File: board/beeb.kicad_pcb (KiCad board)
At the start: 2 copper layers, 59.7 x 53.3 mm, 24 parts, among them J2 AVR-JTAG-10, SW1 SW_DIP_x08, U2 ps2, U3 XC95144XL-TQ100, U4 beebKB, U5 OKI-78SR-3.3_1.5-W36-C

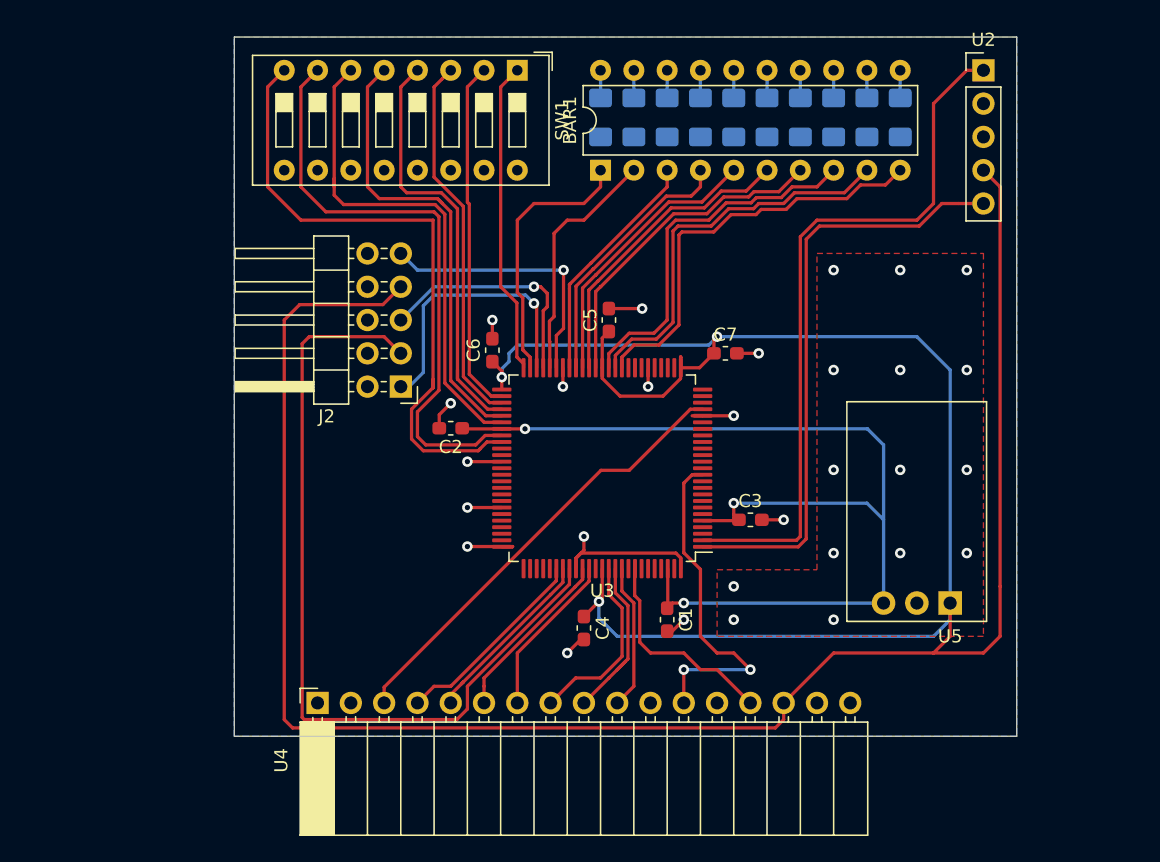
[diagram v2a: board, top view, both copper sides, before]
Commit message: Add ps/2 socket footprint from github. Add USB socket via WIT122 IC.
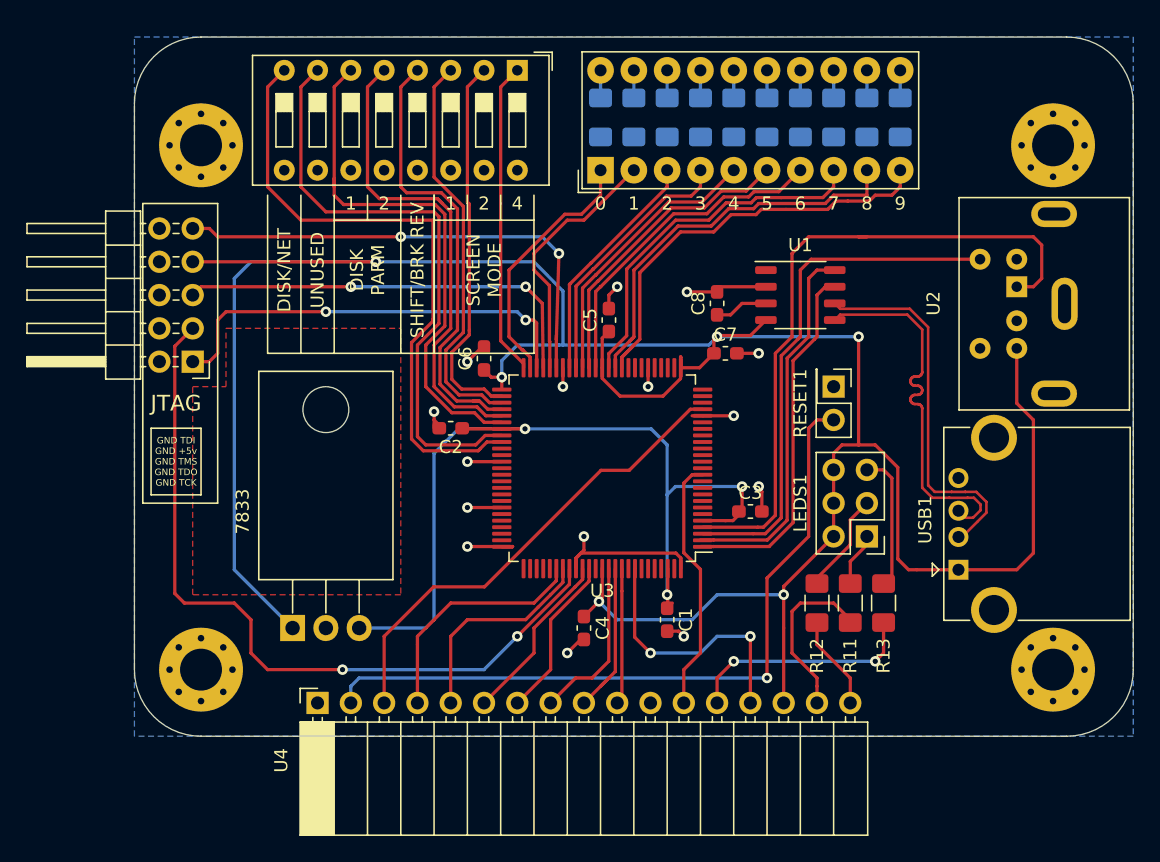
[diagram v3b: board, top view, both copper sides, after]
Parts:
- added C8: 0.1uF, Capacitor_SMD:C_0603_1608Metric_Pad1.05x0.95mm_HandSolder, F.Cu at (91.4, 99.1)
- added H1: MountingHole_Pad, MountingHole:MountingHole_3.2mm_M3_Pad_Via, F.Cu at (117.1, 127.0)
- added H2: MountingHole_Pad, MountingHole:MountingHole_3.2mm_M3_Pad_Via, F.Cu at (117.1, 87.0)
- added H3: MountingHole_Pad, MountingHole:MountingHole_3.2mm_M3_Pad_Via, F.Cu at (52.1, 127.0)
- added H4: MountingHole_Pad, MountingHole:MountingHole_3.2mm_M3_Pad_Via, F.Cu at (52.1, 87.0)
- added LEDS1: J1, Connector_PinHeader_2.54mm:PinHeader_2x03_P2.54mm_Vertical, F.Cu at (102.9, 116.8)
- added R11: 470, Resistor_SMD:R_1206_3216Metric_Pad1.42x1.75mm_HandSolder, F.Cu at (101.6, 121.9)
- added R12: 470, Resistor_SMD:R_1206_3216Metric_Pad1.42x1.75mm_HandSolder, F.Cu at (99.1, 121.9)
- added R13: 470, Resistor_SMD:R_1206_3216Metric_Pad1.42x1.75mm_HandSolder, F.Cu at (104.1, 121.9)
- added RESET1: J3, Connector_PinHeader_2.54mm:PinHeader_2x01_P2.54mm_Vertical, F.Cu at (100.3, 105.4)
- added U1: WIT122UH, Package_SO:SOP-8_3.9x4.9mm_P1.27mm, F.Cu at (97.8, 98.4)
- added USB1: USB, Connector_USB:USB_A_CONNFLY_DS1095-WNR0, F.Cu at (109.9, 119.4)
- BAR1: footprint Package_DIP:DIP-20_W7.62mm -> Display:HDSP-4830
- U2: footprint Connector_PinHeader_2.54mm:PinHeader_1x05_P2.54mm_Vertical -> thirdparty:Connector_Mini-DIN_Female_6Pin_2rows
- U5: value OKI-78SR-3.3_1.5-W36-C -> 7833; footprint Converter_DCDC:Converter_DCDC_muRata_OKI-78SR_Horizontal -> Package_TO_SOT_THT:TO-220-3_Horizontal_TabDown
- moved U5 50.2 mm to (59.1, 123.8), turned to 0 degrees
- moved U2 16.7 mm to (114.3, 97.8), turned to 90 degrees
- moved J2 16.0 mm to (51.4, 103.5)
- moved C6 0.90 mm to (73.7, 103.3)
- moved C3 0.63 mm to (94.0, 114.9)
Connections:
- J2 pad 4: Net-(J2-Pad4) -> (no net)
- J2 pad 6: Net-(J2-Pad6) -> (no net)
- J2 pad 8: Net-(J2-Pad8) -> (no net)
- U2 pad 1: Net-(U2-Pad1) -> /PS2DATA_A
- U2 pad 5: Net-(U2-Pad5) -> /PS2CLK_A
- U3 pad 1: Net-(U2-Pad5) -> /PS2DATA_B
- U3 pad 10: Net-(U3-Pad10) -> (no net)
- U3 pad 11: Net-(U3-Pad11) -> (no net)
- U3 pad 13: Net-(U3-Pad13) -> (no net)
- U3 pad 14: Net-(U3-Pad14) -> (no net)
- U3 pad 15: Net-(U3-Pad15) -> (no net)
- U3 pad 16: Net-(U3-Pad16) -> (no net)
- U3 pad 17: Net-(U3-Pad17) -> (no net)
- U3 pad 18: Net-(U3-Pad18) -> (no net)
- U3 pad 19: Net-(U3-Pad19) -> (no net)
- U3 pad 2: Net-(U2-Pad1) -> /PS2CLK_B
- U3 pad 20: Net-(U3-Pad20) -> (no net)
- U3 pad 23: Net-(U3-Pad23) -> (no net)
- U3 pad 24: Net-(U3-Pad24) -> (no net)
- U3 pad 25: Net-(U3-Pad25) -> (no net)
- U3 pad 27: Net-(U3-Pad27) -> (no net)
- U3 pad 28: Net-(U3-Pad28) -> (no net)
- U3 pad 29: Net-(U3-Pad29) -> (no net)
- U3 pad 3: Net-(U3-Pad3) -> /PS2CLK_A
- U3 pad 30: Net-(U3-Pad30) -> (no net)
- U3 pad 32: Net-(U3-Pad32) -> (no net)
- U3 pad 33: Net-(U3-Pad33) -> (no net)
- U3 pad 34: Net-(U3-Pad34) -> (no net)
- U3 pad 4: Net-(U3-Pad4) -> /PS2DATA_A
- U3 pad 6: Net-(U3-Pad6) -> (no net)
- U3 pad 60: Net-(U3-Pad60) -> (no net)
- U3 pad 61: Net-(U3-Pad61) -> (no net)
- U3 pad 63: Net-(U3-Pad63) -> (no net)
- U3 pad 64: Net-(U3-Pad64) -> (no net)
- U3 pad 65: Net-(U3-Pad65) -> (no net)
- U3 pad 66: Net-(U3-Pad66) -> (no net)
- U3 pad 67: Net-(U3-Pad67) -> (no net)
- U3 pad 68: Net-(U3-Pad68) -> (no net)
- U3 pad 7: Net-(U3-Pad7) -> (no net)
- U3 pad 70: Net-(U3-Pad70) -> (no net)
- U3 pad 71: Net-(U3-Pad71) -> (no net)
- U3 pad 72: Net-(U3-Pad72) -> (no net)
- U3 pad 73: Net-(U3-Pad73) -> (no net)
- U3 pad 74: Net-(U3-Pad74) -> (no net)
- U3 pad 76: Net-(U3-Pad76) -> (no net)
- U3 pad 77: Net-(U3-Pad77) -> (no net)
- U3 pad 78: Net-(U3-Pad78) -> (no net)
- U3 pad 79: Net-(U3-Pad79) -> (no net)
- U3 pad 8: Net-(U3-Pad8) -> (no net)
- U3 pad 80: Net-(U3-Pad80) -> (no net)
- U3 pad 87: /COL3 -> (no net)
- U3 pad 9: Net-(U3-Pad9) -> (no net)
- U3 pad 92: Net-(U3-Pad92) -> (no net)
- U3 pad 94: Net-(U3-Pad94) -> (no net)
- U3 pad 95: Net-(U3-Pad95) -> (no net)
- U3 pad 96: Net-(U3-Pad96) -> (no net)
- U3 pad 97: Net-(U3-Pad97) -> (no net)
- U3 pad 99: Net-(U3-Pad99) -> (no net)
- U4 pad 11: /ROW3 -> (no net)
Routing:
- net Net-(RESET1-Pad2): track 0.00 -> 55.8 mm, vias 0 -> 1
- net Net-(U2-Pad1): track 54.1 -> 0.00 mm
- net /PS2DATA_A: track 0.00 -> 51.6 mm
- net Net-(U2-Pad5): track 45.7 -> 0.00 mm
- net /PS2CLK_A: track 0.00 -> 40.0 mm
- net +5V: track 249.2 -> 217.2 mm, vias 3 -> 6
- net /USB_P: track 0.00 -> 28.6 mm
- net /USB_N: track 0.00 -> 28.6 mm
- net /PS2CLK_B: track 0.00 -> 28.6 mm
- net /PS2DATA_B: track 0.00 -> 27.6 mm
- net Net-(R13-Pad2): track 0.00 -> 17.7 mm, vias 0 -> 2
- net /TDI: track 20.6 -> 37.7 mm, vias 1 -> 2
- net /TMS: track 18.9 -> 32.4 mm, vias 1 -> 2
- net Net-(R11-Pad2): track 0.00 -> 13.2 mm
- net +3V3: track 80.6 -> 68.8 mm
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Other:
- board size 59.7 x 53.3 mm -> 76.2 x 53.3 mm
- board text added: "0"
- board text added: "1"
- board text added: "2"
- board text added: "3"
- board text added: "4"
- board text added: "5"
- board text added: "6"
- board text added: "7"
- board text added: "8"
- board text added: "9"
- board text added: "BBC Micro to PS/2 and USB keyboard"
- board text added: "BUILD_XXXXX"
- board text added: "DISK PARM"
- board text added: "DISK/NET"
- board text added: "GIT_XXXXX"
- board text added: "GND TDI GND +5v GND TMS GND TDO GND TCK"
- board text added: "JTAG"
- board text added: "SCREEN MODE"
- board text added: "SHIFT/BRK REV"
- board text added: "UNUSED"

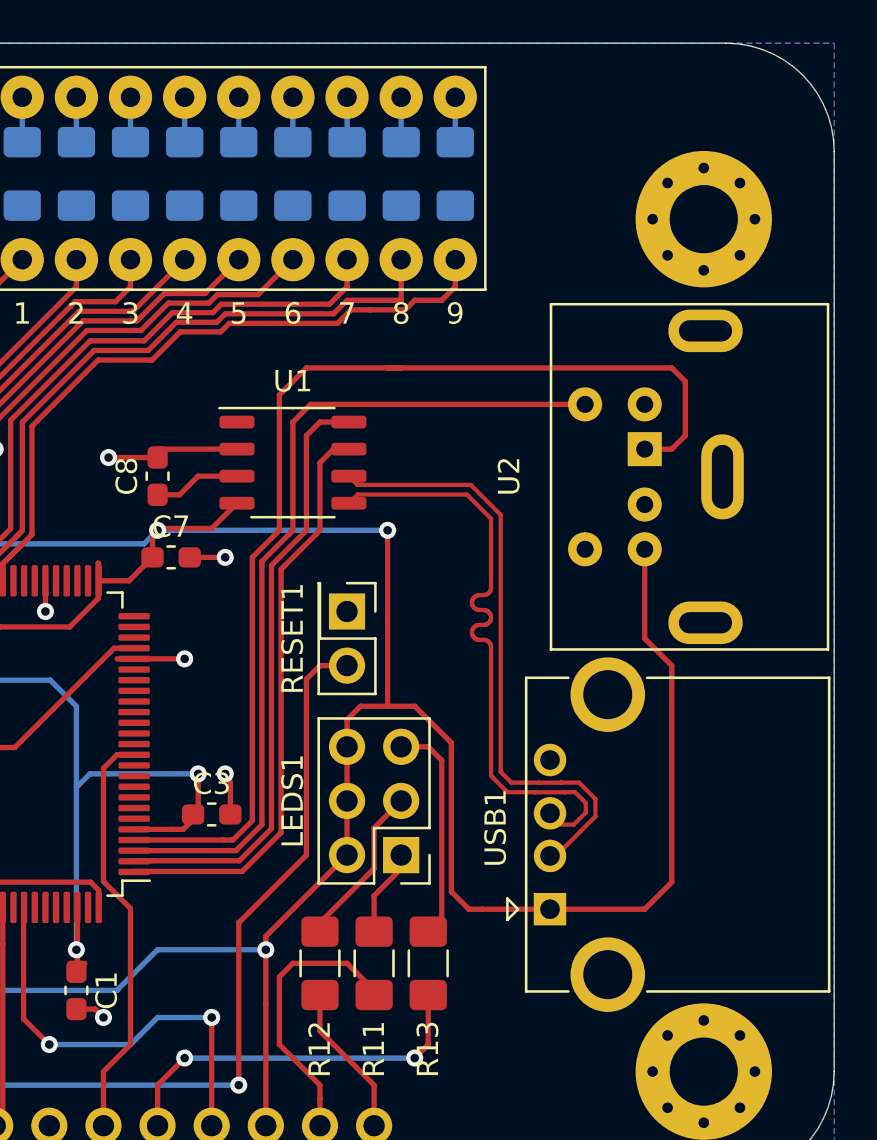
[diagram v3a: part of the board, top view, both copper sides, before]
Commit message: Change USB socket footprint, impedence match usb p/n and ps2 clk/data
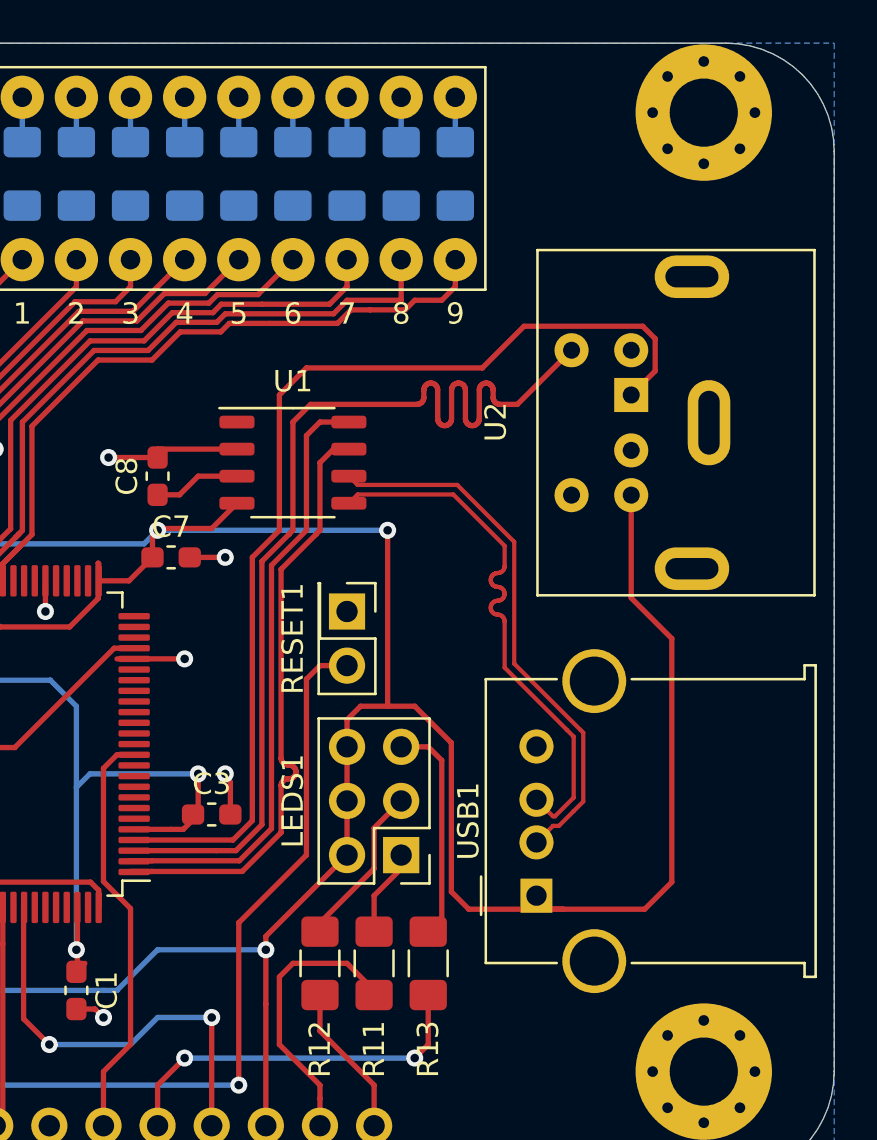
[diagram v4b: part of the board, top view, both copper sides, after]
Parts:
- USB1: footprint Connector_USB:USB_A_CONNFLY_DS1095-WNR0 -> Connector_USB:USB_A_Molex_67643_Horizontal
- moved H2 5.00 mm to (117.1, 82.0)
- moved U2 2.62 mm to (113.7, 95.2)
- moved USB1 0.90 mm to (109.2, 118.7)
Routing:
- net /PS2CLK_A: track 40.0 -> 48.8 mm
- net /USB_P: track 28.6 -> 25.6 mm
- net /USB_N: track 28.6 -> 25.6 mm
- net /PS2DATA_A: track 51.6 -> 48.7 mm
- net +5V: track 217.2 -> 219.7 mm
- net /PS2DATA_B: track 27.6 -> 28.4 mm

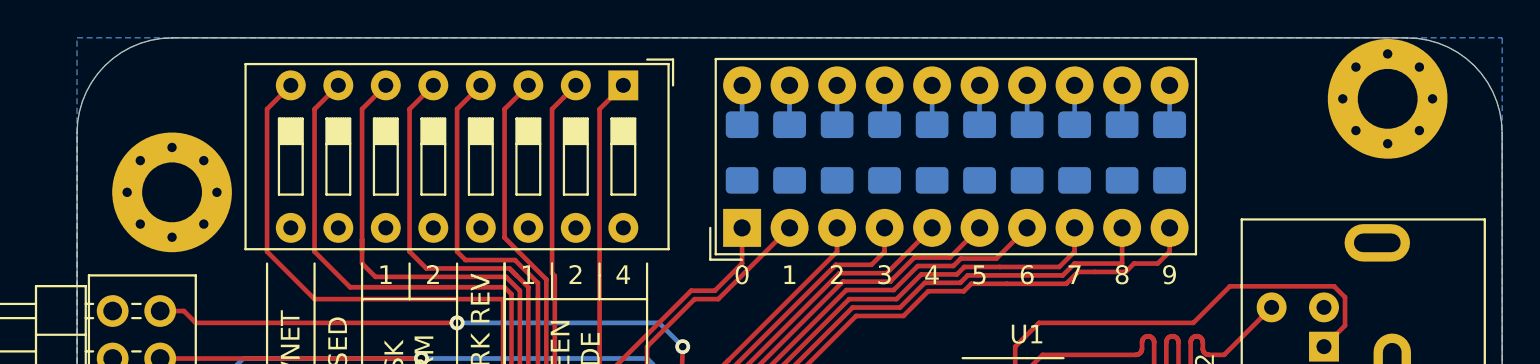
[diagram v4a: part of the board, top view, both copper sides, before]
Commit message: tweak hole placement
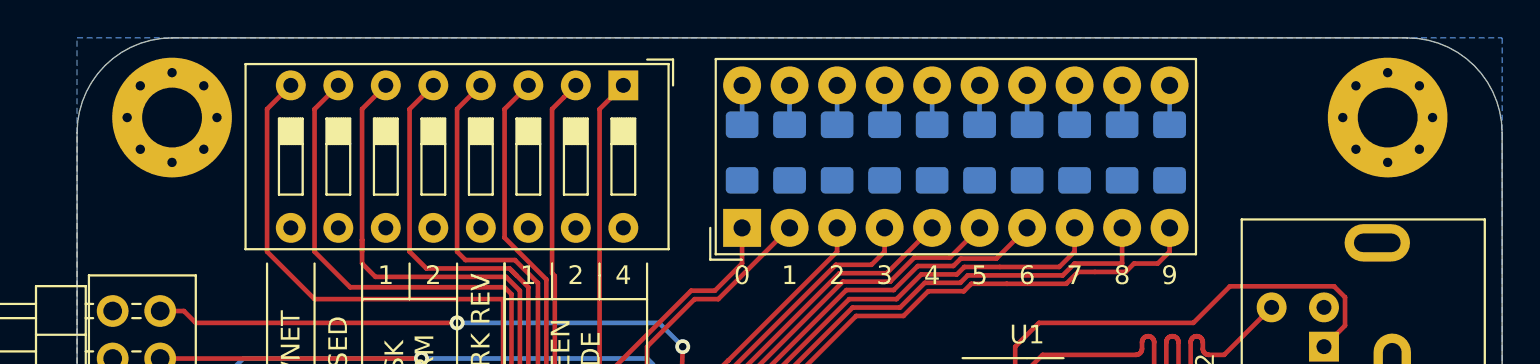
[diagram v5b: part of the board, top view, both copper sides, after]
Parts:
- moved H4 4.00 mm to (52.1, 83.0)
- moved H2 1.00 mm to (117.1, 83.0)

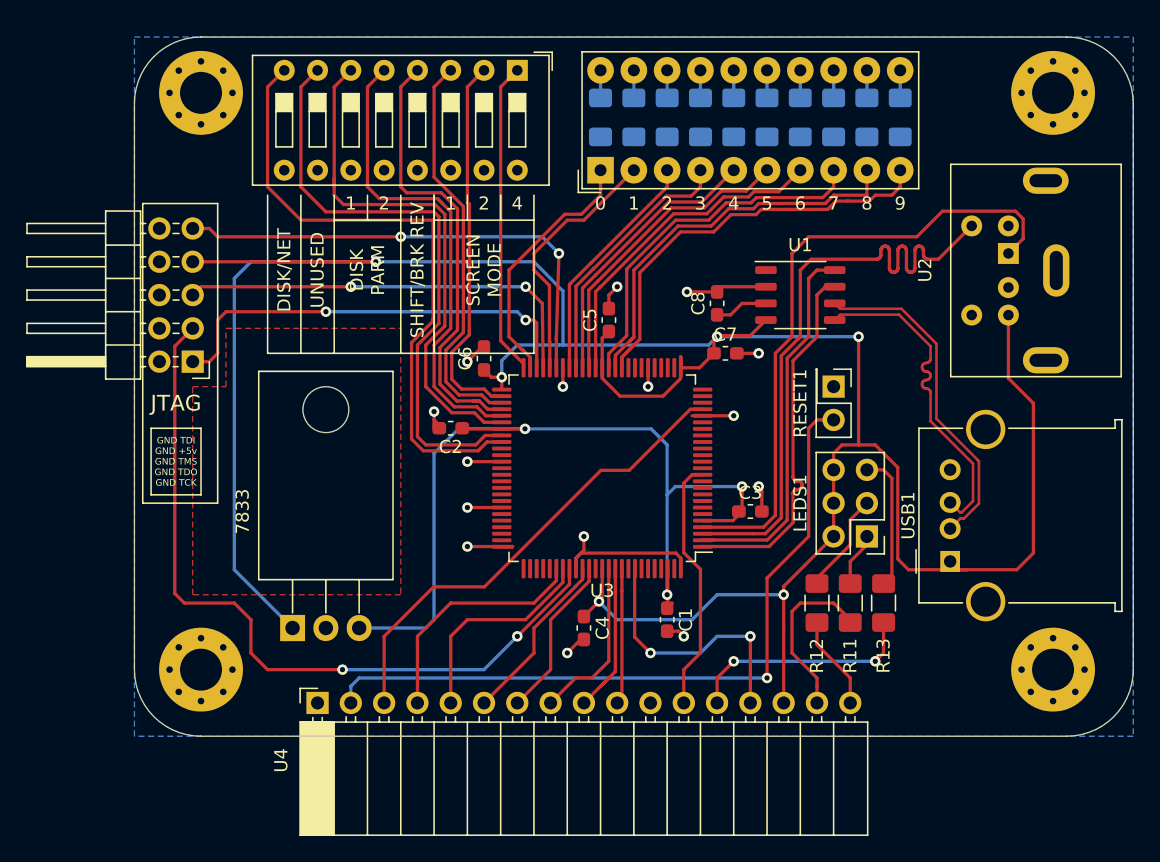
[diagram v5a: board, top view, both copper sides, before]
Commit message: connect CPLD vio to 3.3v, change 3.3v reg to lm1117t
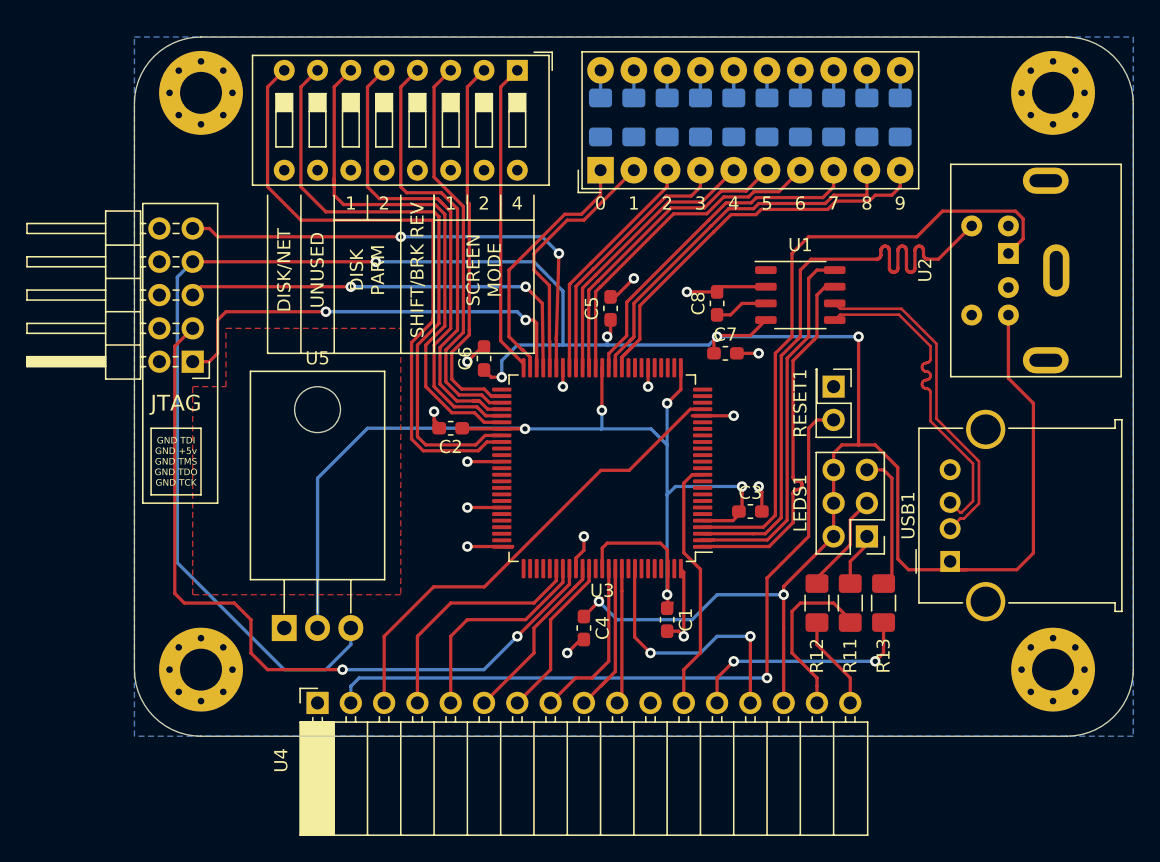
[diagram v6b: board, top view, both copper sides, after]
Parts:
- U5: value 7833 -> LM1117-3.3
- moved C5 0.90 mm to (83.3, 99.4)
- moved U5 0.63 mm to (58.4, 123.8)
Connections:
- U3 pad 26: +5V -> +3V3
- U3 pad 38: +5V -> +3V3
- U3 pad 51: +5V -> +3V3
- U3 pad 88: +5V -> +3V3
- U5 pad 1: +5V -> GND
- U5 pad 2: GND -> +3V3
- U5 pad 3: +3V3 -> +5V
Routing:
- net +3V3: track 68.8 -> 92.6 mm, vias 3 -> 5
- net +5V: track 219.7 -> 204.5 mm, vias 6 -> 7
- net GND: track 46.8 -> 43.4 mm
- net /LED9: track 30.4 -> 28.9 mm
- net /LED8: track 27.7 -> 26.3 mm
- net /LED10: track 33.0 -> 31.5 mm

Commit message: fix unconnected pad
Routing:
- net +3V3: track 92.6 -> 97.0 mm

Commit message: Connect jtag connector to 3v3
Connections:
- J2 pad 4: (no net) -> +3V3
- J2 pad 7: +5V -> +3V3
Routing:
- net +5V: track 204.5 -> 148.2 mm, vias 7 -> 6
- net +3V3: track 97.0 -> 121.6 mm
